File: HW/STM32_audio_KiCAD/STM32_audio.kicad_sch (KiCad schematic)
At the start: 85 parts, among them J1 Screw_Terminal_01x02, J2 SWD, J4 Conn_01x04, J5 USB_B_Mini, J6 AudioJack3_Ground, J7 Micro_SD_Card_Det2, J8 KY-018, J9 OLED_0,96", Q1 AO3401A, SW1 SW_SPDT, SW2 SW_Push, U1 STM32F405RGT6, U3 USBLC6-2SC6, U4 PCM5102A, Y1 16MHz

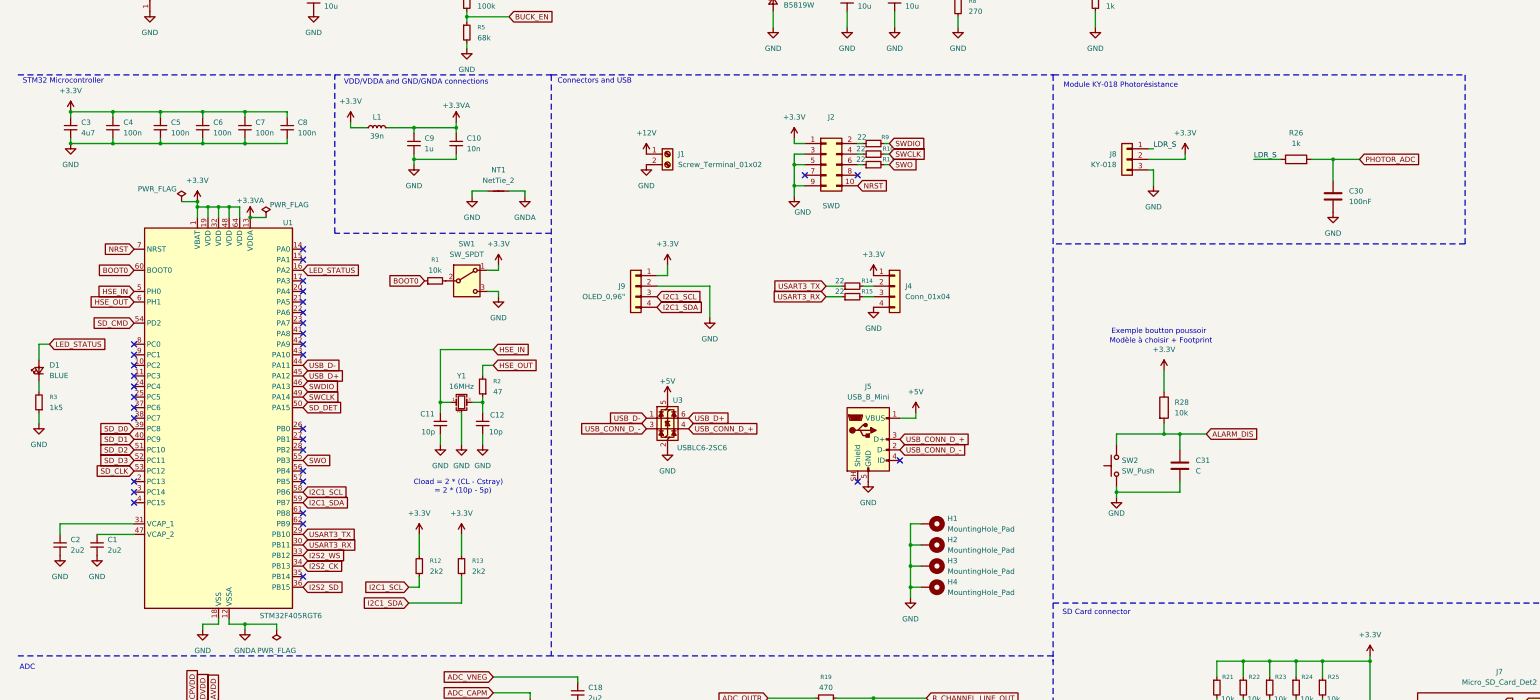
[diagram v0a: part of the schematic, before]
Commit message: Ajout capteur de lumière
- Removed photoresistor
- Added TSL25911FN and related pull-ups
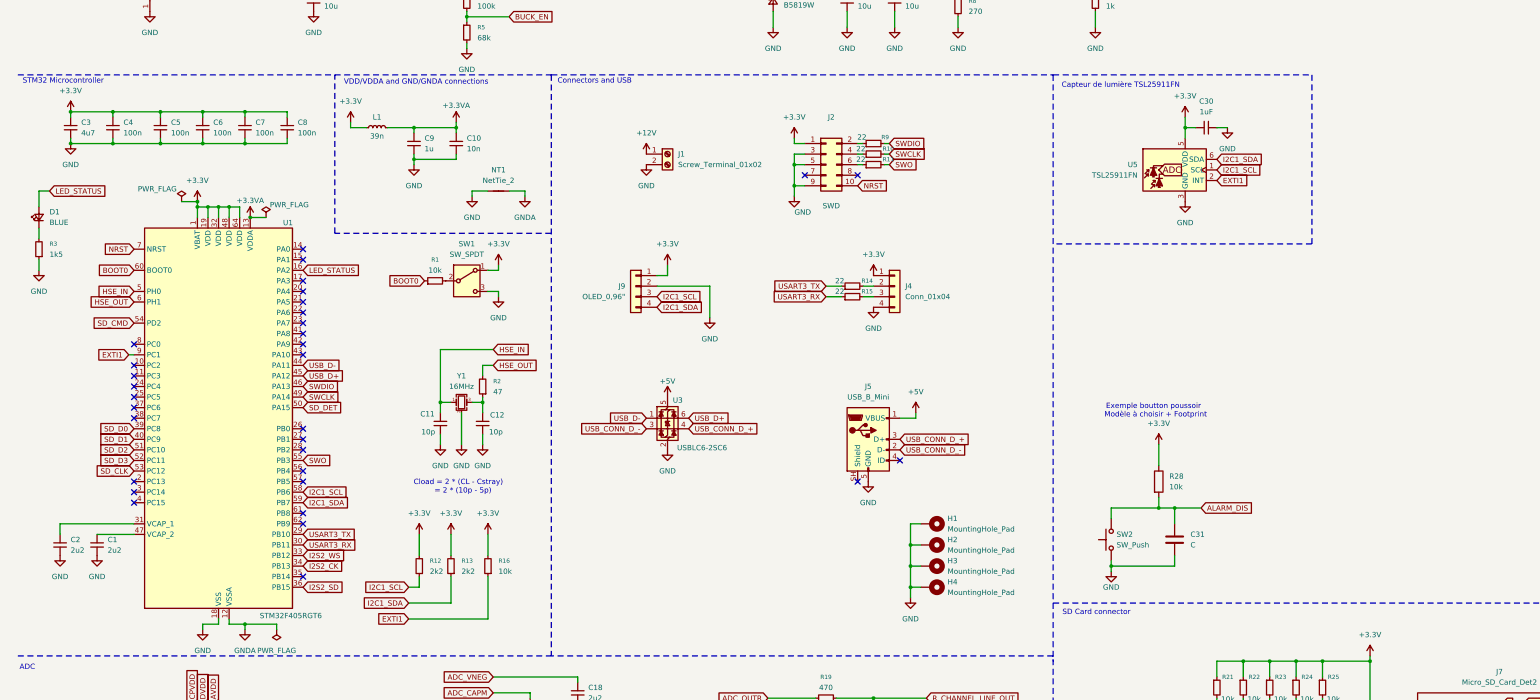
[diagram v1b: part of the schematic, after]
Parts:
- removed C30: 100nF, Capacitor_SMD:C_0805_2012Metric, symbol Device:C
- removed J8: KY-018, symbol Connector_Generic:Conn_01x03
- removed R26: 1k, Resistor_SMD:R_0805_2012Metric, symbol Device:R
- added C30: 1uF, OptoDevice:AMS_TSL25911FN, symbol Device:C_Small
- added R16: 10k, Resistor_THT:R_Array_SIP4, symbol Device:R_Small
- added U5: TSL25911FN, OptoDevice:AMS_TSL25911FN, symbol Sensor_Optical:TSL25911FN
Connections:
- net +3.3V: now also C30.1, R16.2, U5.5 (VDD)
- net GND: now also C30.2, U5.3 (GND)
- net I2C1_SCL: now also U5.1 (SCL)
- net I2C1_SDA: now also U5.6 (SDA)
- net EXTI1: now reaches U1.9 (PC1)
- net EXTI1: now also R16.1, U5.2 (INT)
- no-connect marks 33 -> 32
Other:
- note added: "Capteur de lumière TSL25911FN"
- note removed: "Module KY-018 Photorésistance"
- moved on the sheet: C31, D1, R13, R28, R3, SW2
